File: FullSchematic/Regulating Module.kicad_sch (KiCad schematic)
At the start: 7 parts, among them U2 LM1117-3.3

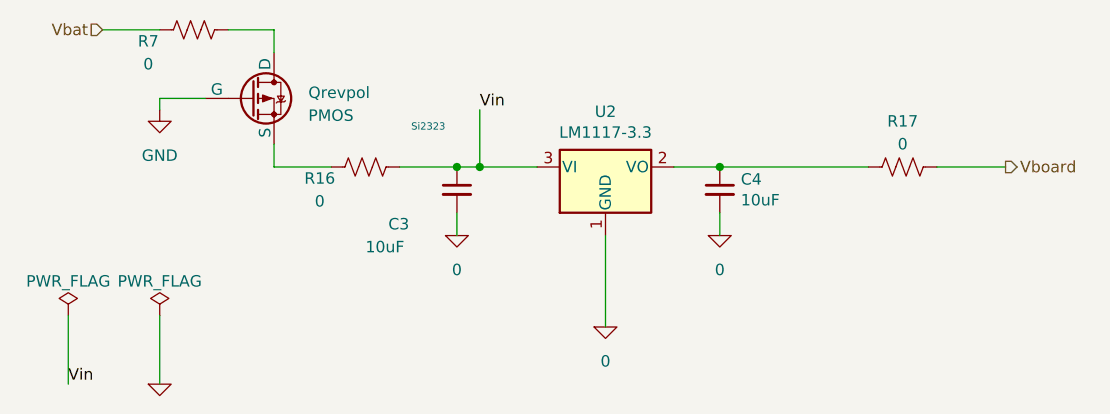
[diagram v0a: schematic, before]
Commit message: Added uvlo circuit
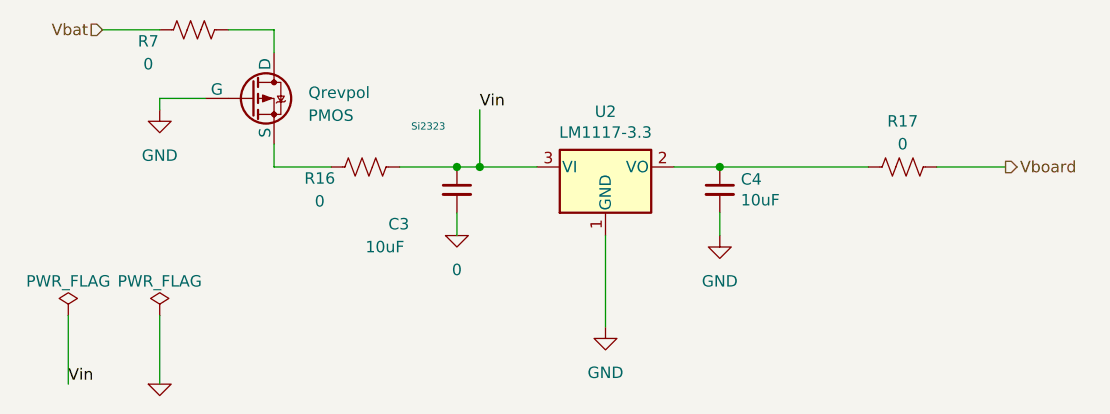
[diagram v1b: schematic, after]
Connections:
- net 0: no longer C4.2, U2.1 (GND)
- net GND: now also C4.2, U2.1 (GND)
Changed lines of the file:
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@@
-    )
-  )
-  (symbol (lib_id "Power module-rescue:0-pspice") (at 133.35 110.49 0) (unit 1)
-    (in_bom yes) (on_board yes) (dnp no)
-    (property "Reference" "#GND0106" (at 133.35 113.03 0)
-      (effects (font (size 1.27 1.27)) hide)
-    )
-    (property "Value" "0" (at 133.35 114.3 0)
-      (effects (font (size 1.27 1.27)))
-    )
-    (property "Footprint" "" (at 133.35 110.49 0)
-      (effects (font (size 1.27 1.27)) hide)
-    )
-    (property "Datasheet" "~" (at 133.35 110.49 0)
-      (effects (font (size 1.27 1.27)) hide)
-    )
-    (pin "1")
-    (instances
-      (project "Power module"
-        (path "/4323dbc9-3623-4dbc-9566-44afc0929253/00000000-0000-0000-0000-00006405027d"
-          (reference "#GND0106") (unit 1)
-        )
-      )
-      (project "FullSchematic"
-        (path "/5dd86611-a33d-45ee-946c-01c599f30b12/58d1f368-4b84-4dfe-a353-084728cf6b07/00000000-0000-0000-0000-00006405027d"
-          (reference "#GND0106") (unit 1)
-        )
-      )
     )
   )
@@
     )
   )
-  (symbol (lib_id "Power module-rescue:0-pspice") (at 146.05 100.33 0) (unit 1)
-    (in_bom yes) (on_board yes) (dnp no)
-    (property "Reference" "#GND0108" (at 146.05 102.87 0)
-      (effects (font (size 1.27 1.27)) hide)
-    )
-    (property "Value" "0" (at 146.05 104.14 0)
-      (effects (font (size 1.27 1.27)))
-    )
-    (property "Footprint" "" (at 146.05 100.33 0)
-      (effects (font (size 1.27 1.27)) hide)
-    )
-    (property "Datasheet" "~" (at 146.05 100.33 0)
-      (effects (font (size 1.27 1.27)) hide)
-    )
-    (pin "1")
-    (instances
-      (project "Power module"
-        (path "/4323dbc9-3623-4dbc-9566-44afc0929253/00000000-0000-0000-0000-00006405027d"
-          (reference "#GND0108") (unit 1)
-        )
-      )
-      (project "FullSchematic"
-        (path "/5dd86611-a33d-45ee-946c-01c599f30b12/58d1f368-4b84-4dfe-a353-084728cf6b07/00000000-0000-0000-0000-00006405027d"
-          (reference "#GND0108") (unit 1)
-        )
-      )
-    )
-  )
   (symbol (lib_id "Device:R_US") (at 166.37 92.71 90) (unit 1)
     (in_bom yes) (on_board yes) (dnp no) (fields_autoplaced)
@@
         )
       )
+    )
+  )
+  (symbol (lib_id "power:GND") (at 133.35 110.49 0) (unit 1)
+    (in_bom yes) (on_board yes) (dnp no) (fields_autoplaced)
+    (property "Reference" "#PWR04" (at 133.35 116.84 0)
+      (effects (font (size 1.27 1.27)) hide)
+    )
+    (property "Value" "GND" (at 133.35 115.57 0)
+      (effects (font (size 1.27 1.27)))
+    )
+    (property "Footprint" "" (at 133.35 110.49 0)
+      (effects (font (size 1.27 1.27)) hide)
+    )
+    (property "Datasheet" "" (at 133.35 110.49 0)
+      (effects (font (size 1.27 1.27)) hide)
+    )
+    (pin "1")
+    (instances
+      (project "Power module"
+        (path "/4323dbc9-3623-4dbc-9566-44afc0929253/00000000-0000-0000-0000-0000640501de"
+          (reference "#PWR04") (unit 1)
+        )
+        (path "/4323dbc9-3623-4dbc-9566-44afc0929253/00000000-0000-0000-0000-00006405027d"
+          (reference "#PWR05") (unit 1)
+        )
+      )
+      (project "FullSchematic"
+        (path "/5dd86611-a33d-45ee-946c-01c599f30b12/58d1f368-4b84-4dfe-a353-084728cf6b07/00000000-0000-0000-0000-00006405027d"
+          (reference "#PWR016") (unit 1)
+        )
+      )
+    )
+  )
+  (symbol (lib_id "power:GND") (at 146.05 100.33 0) (unit 1)
+    (in_bom yes) (on_board yes) (dnp no) (fields_autoplaced)
+    (property "Reference" "#PWR04" (at 146.05 106.68 0)
+      (effects (font (size 1.27 1.27)) hide)
+    )
+    (property "Value" "GND" (at 146.05 105.41 0)
+      (effects (font (size 1.27 1.27)))
+    )
+    (property "Footprint" "" (at 146.05 100.33 0)
+      (effects (font (size 1.27 1.27)) hide)
+    )
+    (property "Datasheet" "" (at 146.05 100.33 0)
+      (effects (font (size 1.27 1.27)) hide)
+    )
+    (pin "1")
+    (instances
+      (project "Power module"
+        (path "/4323dbc9-3623-4dbc-9566-44afc0929253/00000000-0000-0000-0000-0000640501de"
+          (reference "#PWR04") (unit 1)
+        )
+        (path "/4323dbc9-3623-4dbc-9566-44afc0929253/00000000-0000-0000-0000-00006405027d"
+          (reference "#PWR05") (unit 1)
+        )
+      )
+      (project "FullSchematic"
+        (path "/5dd86611-a33d-45ee-946c-01c599f30b12/58d1f368-4b84-4dfe-a353-084728cf6b07/00000000-0000-0000-0000-00006405027d"
+          (reference "#PWR017") (unit 1)
+        )
+      )

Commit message: Confirmed part numbers and prices
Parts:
- C3, C4: footprint Library:CAPC1608X90N -> Capacitor_SMD:C_0603_1608Metric; Populate (none) -> Yes
- Qrevpol, U2: Populate (none) -> Yes
- R16, R17, R7: footprint Library:RESC2013X65N -> Resistor_SMD:R_1206_3216Metric; Populate (none) -> Yes
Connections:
- net 0: no longer C3.2
- net GND: now also C3.2
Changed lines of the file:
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@@
+      (effects (font (size 1.27 1.27)) hide)
+    )
+    (property "Populate" "Yes" (at 133.35 92.71 0)
       (effects (font (size 1.27 1.27)) hide)
     )
@@
       (effects (font (size 1.27 1.27)) (justify left))
     )
-    (property "Footprint" "Library:CAPC1608X90N" (at 116.84 95.25 0)
+    (property "Footprint" "Capacitor_SMD:C_0603_1608Metric" (at 116.84 95.25 0)
       (effects (font (size 1.27 1.27)) hide)
     )
@@
     )
     (property "JLCPCB Part #" "C1691" (at 116.84 95.25 0)
+      (effects (font (size 1.27 1.27)) hide)
+    )
+    (property "Populate" "Yes" (at 116.84 95.25 0)
       (effects (font (size 1.27 1.27)) hide)
     )
@@
       (effects (font (size 1.27 1.27)) (justify left))
     )
-    (property "Footprint" "Library:CAPC1608X90N" (at 146.05 95.25 0)
+    (property "Footprint" "Capacitor_SMD:C_0603_1608Metric" (at 146.05 95.25 0)
       (effects (font (size 1.27 1.27)) hide)
     )
@@
       (effects (font (size 1.27 1.27)) hide)
     )
+    (property "Populate" "Yes" (at 146.05 95.25 0)
+      (effects (font (size 1.27 1.27)) hide)
+    )
     (pin "1")
     (pin "2")
@@
     )
   )
-  (symbol (lib_id "Power module-rescue:0-pspice") (at 116.84 100.33 0) (unit 1)
-    (in_bom yes) (on_board yes) (dnp no)
-    (property "Reference" "#GND0107" (at 116.84 102.87 0)
-      (effects (font (size 1.27 1.27)) hide)
-    )
-    (property "Value" "0" (at 116.84 104.14 0)
-      (effects (font (size 1.27 1.27)))
-    )
-    (property "Footprint" "" (at 116.84 100.33 0)
-      (effects (font (size 1.27 1.27)) hide)
-    )
-    (property "Datasheet" "~" (at 116.84 100.33 0)
-      (effects (font (size 1.27 1.27)) hide)
-    )
-    (pin "1")
-    (instances
-      (project "Power module"
-        (path "/4323dbc9-3623-4dbc-9566-44afc0929253/00000000-0000-0000-0000-00006405027d"
-          (reference "#GND0107") (unit 1)
-        )
-      )
-      (project "FullSchematic"
-        (path "/5dd86611-a33d-45ee-946c-01c599f30b12/58d1f368-4b84-4dfe-a353-084728cf6b07/00000000-0000-0000-0000-00006405027d"
-          (reference "#GND0107") (unit 1)
-        )
-      )
-    )
-  )
   (symbol (lib_id "Device:R_US") (at 166.37 92.71 90) (unit 1)
     (in_bom yes) (on_board yes) (dnp no) (fields_autoplaced)
@@
       (effects (font (size 1.27 1.27)))
     )
-    (property "Footprint" "Library:RESC2013X65N" (at 166.624 91.694 90)
+    (property "Footprint" "Resistor_SMD:R_1206_3216Metric" (at 166.624 91.694 90)
       (effects (font (size 1.27 1.27)) hide)
     )
@@
       (effects (font (size 1.27 1.27)) hide)
     )
+    (property "Populate" "Yes" (at 166.37 92.71 0)
+      (effects (font (size 1.27 1.27)) hide)
+    )
     (pin "1")
     (pin "2")
@@
     )
     (property "Price" "0.09" (at 93.98 85.09 0)
+      (effects (font (size 1.27 1.27)) hide)
+    )
+    (property "Populate" "Yes" (at 93.98 85.09 0)
       (effects (font (size 1.27 1.27)) hide)
     )
@@
       (effects (font (size 1.27 1.27)))
     )
-    (property "Footprint" "Library:RESC2013X65N" (at 87.884 76.454 90)
+    (property "Footprint" "Resistor_SMD:R_1206_3216Metric" (at 87.884 76.454 90)
       (effects (font (size 1.27 1.27)) hide)
     )
@@
     )
     (property "Price (5 boards)" "0.06" (at 87.63 77.47 0)
+      (effects (font (size 1.27 1.27)) hide)
+    )
+    (property "Populate" "Yes" (at 87.63 77.47 0)
       (effects (font (size 1.27 1.27)) hide)
     )
@@
       (effects (font (size 1.27 1.27)))
     )
-    (property "Footprint" "Library:RESC2013X65N" (at 106.934 91.694 90)
+    (property "Footprint" "Resistor_SMD:R_1206_3216Metric" (at 106.934 91.694 90)
       (effects (font (size 1.27 1.27)) hide)
     )
@@
       (effects (font (size 1.27 1.27)) hide)
     )
+    (property "Populate" "Yes" (at 106.68 92.71 0)
+      (effects (font (size 1.27 1.27)) hide)
+    )
     (pin "1")
     (pin "2")
@@
         )
       )
+    )
+  )
+  (symbol (lib_id "power:GND") (at 116.84 100.33 0) (unit 1)
+    (in_bom yes) (on_board yes) (dnp no) (fields_autoplaced)
+    (property "Reference" "#PWR021" (at 116.84 106.68 0)
+      (effects (font (size 1.27 1.27)) hide)
+    )
+    (property "Value" "GND" (at 116.84 105.41 0)
+      (effects (font (size 1.27 1.27)))
+    )
+    (property "Footprint" "" (at 116.84 100.33 0)
+      (effects (font (size 1.27 1.27)) hide)
+    )
+    (property "Datasheet" "" (at 116.84 100.33 0)
+      (effects (font (size 1.27 1.27)) hide)
+    )
+    (pin "1")
+    (instances
+      (project "FullSchematic"
+        (path "/5dd86611-a33d-45ee-946c-01c599f30b12/58d1f368-4b84-4dfe-a353-084728cf6b07/00000000-0000-0000-0000-00006405027d"
+          (reference "#PWR021") (unit 1)
+        )
+      )

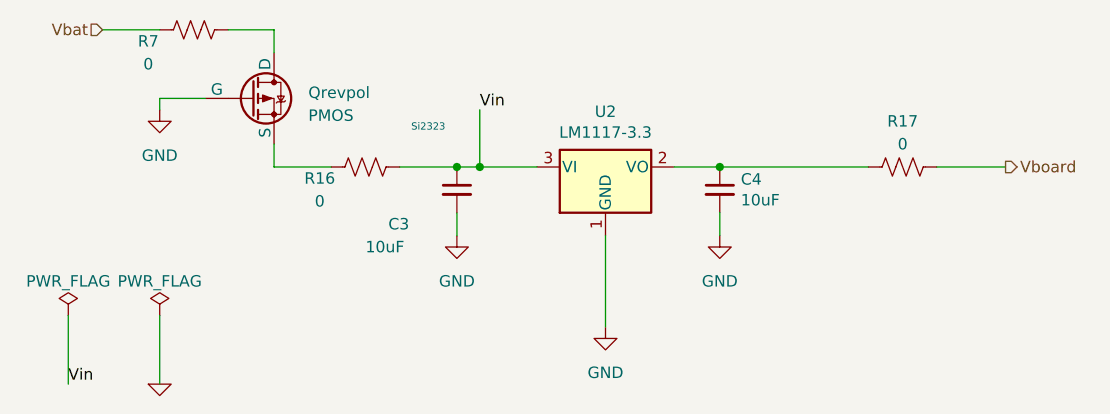
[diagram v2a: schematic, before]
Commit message: Checked part #s, prices, footprints
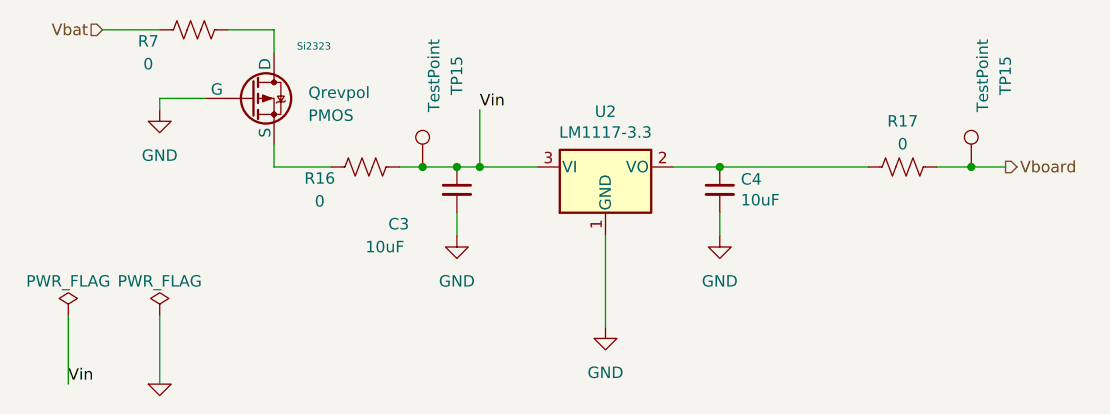
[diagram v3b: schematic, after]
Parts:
- added TP15 (x2): TestPoint, TestPoint:TestPoint_Pad_D2.0mm, symbol Connector:TestPoint
- C3: Price 0.08 -> 0.0052; Price ( 1 board) 0.24 -> 0.0208; Price (5 boards) 1.20 -> 0.104
- C4: Price 0.01 -> 0.0052; Price ( 1 board) 0.01 -> 0.0208; Price (5 boards) 0.05 -> 0.104
- Qrevpol: Price 0.09 -> 0.0721; Price ( 1 board) 0.18 -> 0.1442; Price (5 boards) 0.9 -> 0.721
- R16, R17, R7: Price ( 1 board) 0.012 -> 0.018; Price (5 boards) 0.06 -> 0.09
- U2: Price 0.072 -> 0.1455; Price ( 1 board) 0.072 -> 0.1455; Price (5 boards) 0.36 -> 0.7275
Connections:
- net Vboard: now also TP15.1
- net Vin: now also TP15.1
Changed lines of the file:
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@@
   (junction (at 146.05 92.71) (diameter 0) (color 0 0 0 0)
   )
+  (junction (at 113.03 92.71) (diameter 0) (color 0 0 0 0)
+  )
+  (junction (at 173.99 92.71) (diameter 0) (color 0 0 0 0)
+  )
   (junction (at 116.84 92.71) (diameter 0) (color 0 0 0 0)
   )
@@
     (stroke (width 0) (type default))
   )
-  (wire (pts (xy 110.49 92.71) (xy 116.84 92.71))
+  (wire (pts (xy 110.49 92.71) (xy 113.03 92.71))
     (stroke (width 0) (type default))
   )
@@
     (stroke (width 0) (type default))
   )
+  (wire (pts (xy 173.99 92.71) (xy 177.8 92.71))
+    (stroke (width 0) (type default))
+  )
   (wire (pts (xy 77.47 77.47) (xy 83.82 77.47))
     (stroke (width 0) (type default))
@@
     (stroke (width 0) (type default))
   )
-  (wire (pts (xy 170.18 92.71) (xy 177.8 92.71))
+  (wire (pts (xy 170.18 92.71) (xy 173.99 92.71))
     (stroke (width 0) (type default))
   )
@@
     (stroke (width 0) (type default))
   )
+  (wire (pts (xy 113.03 92.71) (xy 116.84 92.71))
+    (stroke (width 0) (type default))
+  )
   (wire (pts (xy 73.66 109.22) (xy 73.66 116.84))
     (stroke (width 0) (type default))
@@
     (stroke (width 0) (type default))
   )
-  (text "Si2323" (at 111.76 88.9 0)
+  (text "Si2323" (at 99.06 80.01 0)
     (effects (font (size 0.8 0.8)) (justify left bottom))
   )
@@
       (effects (font (size 1.27 1.27)) hide)
     )
-    (property "Price" "0.072" (at 133.35 92.71 0)
-      (effects (font (size 1.27 1.27)) hide)
-    )
-    (property "Price ( 1 board)" "0.072" (at 133.35 92.71 0)
-      (effects (font (size 1.27 1.27)) hide)
-    )
-    (property "Price (5 boards)" "0.36" (at 133.35 92.71 0)
+    (property "Price" "0.1455" (at 133.35 92.71 0)
+      (effects (font (size 1.27 1.27)) hide)
+    )
+    (property "Price ( 1 board)" "0.1455" (at 133.35 92.71 0)
+      (effects (font (size 1.27 1.27)) hide)
+    )
+    (property "Price (5 boards)" "0.7275" (at 133.35 92.71 0)
       (effects (font (size 1.27 1.27)) hide)
     )
@@
       (effects (font (size 1.27 1.27)) hide)
     )
-    (property "Price" "0.08" (at 116.84 95.25 0)
-      (effects (font (size 1.27 1.27)) hide)
-    )
-    (property "Price ( 1 board)" "0.24" (at 116.84 95.25 0)
-      (effects (font (size 1.27 1.27)) hide)
-    )
-    (property "Price (5 boards)" "1.20" (at 116.84 95.25 0)
+    (property "Price" "0.0052" (at 116.84 95.25 0)
+      (effects (font (size 1.27 1.27)) hide)
+    )
+    (property "Price ( 1 board)" "0.0208" (at 116.84 95.25 0)
+      (effects (font (size 1.27 1.27)) hide)
+    )
+    (property "Price (5 boards)" "0.104" (at 116.84 95.25 0)
       (effects (font (size 1.27 1.27)) hide)
     )
@@
       (effects (font (size 1.27 1.27)) hide)
     )
-    (property "Price" "0.01" (at 146.05 95.25 0)
-      (effects (font (size 1.27 1.27)) hide)
-    )
-    (property "Price ( 1 board)" "0.01" (at 146.05 95.25 0)
-      (effects (font (size 1.27 1.27)) hide)
-    )
-    (property "Price (5 boards)" "0.05" (at 146.05 95.25 0)
+    (property "Price" "0.0052" (at 146.05 95.25 0)
+      (effects (font (size 1.27 1.27)) hide)
+    )
+    (property "Price ( 1 board)" "0.0208" (at 146.05 95.25 0)
+      (effects (font (size 1.27 1.27)) hide)
+    )
+    (property "Price (5 boards)" "0.104" (at 146.05 95.25 0)
       (effects (font (size 1.27 1.27)) hide)
     )
@@
       (effects (font (size 1.27 1.27)) hide)
     )
-    (property "Price ( 1 board)" "0.012" (at 166.37 92.71 0)
-      (effects (font (size 1.27 1.27)) hide)
-    )
-    (property "Price (5 boards)" "0.06" (at 166.37 92.71 0)
+    (property "Price ( 1 board)" "0.018" (at 166.37 92.71 0)
+      (effects (font (size 1.27 1.27)) hide)
+    )
+    (property "Price (5 boards)" "0.09" (at 166.37 92.71 0)
       (effects (font (size 1.27 1.27)) hide)
     )
@@
       (effects (font (size 1.27 1.27)) hide)
     )
-    (property "Price ( 1 board)" "0.18" (at 93.98 85.09 0)
-      (effects (font (size 1.27 1.27)) hide)
-    )
-    (property "Price (5 boards)" "0.9" (at 93.98 85.09 0)
+    (property "Price ( 1 board)" "0.1442" (at 93.98 85.09 0)
+      (effects (font (size 1.27 1.27)) hide)
+    )
+    (property "Price (5 boards)" "0.721" (at 93.98 85.09 0)
       (effects (font (size 1.27 1.27)) hide)
     )
@@
       (effects (font (size 1.27 1.27)) hide)
     )
-    (property "Price" "0.09" (at 93.98 85.09 0)
+    (property "Price" "0.0721" (at 93.98 85.09 0)
       (effects (font (size 1.27 1.27)) hide)
     )
@@
       (effects (font (size 1.27 1.27)) hide)
     )
-    (property "Price ( 1 board)" "0.012" (at 87.63 77.47 0)
-      (effects (font (size 1.27 1.27)) hide)
-    )
-    (property "Price (5 boards)" "0.06" (at 87.63 77.47 0)
+    (property "Price ( 1 board)" "0.018" (at 87.63 77.47 0)
+      (effects (font (size 1.27 1.27)) hide)
+    )
+    (property "Price (5 boards)" "0.09" (at 87.63 77.47 0)
       (effects (font (size 1.27 1.27)) hide)
     )
@@
     )
   )
+  (symbol (lib_id "Connector:TestPoint") (at 113.03 92.71 0) (unit 1)
+    (in_bom yes) (on_board yes) (dnp no)
+    (property "Reference" "TP15" (at 116.84 82.55 90)
+      (effects (font (size 1.27 1.27)))
+    )
+    (property "Value" "TestPoint" (at 114.3 82.55 90)
+      (effects (font (size 1.27 1.27)))
+    )
+    (property "Footprint" "TestPoint:TestPoint_Pad_D2.0mm" (at 118.11 92.71 0)
+      (effects (font (size 1.27 1.27)) hide)
+    )
+    (property "Datasheet" "~" (at 118.11 92.71 0)
+      (effects (font (size 1.27 1.27)) hide)
+    )
+    (property "Price" "$0" (at 113.03 92.71 0)
+      (effects (font (size 1.27 1.27)) hide)
+    )
+    (property "Price ( 1 board)" "0" (at 113.03 92.71 0)
+      (effects (font (size 1.27 1.27)) hide)
+    )
+    (property "Price (5 boards)" "0" (at 113.03 92.71 0)
+      (effects (font (size 1.27 1.27)) hide)
+    )
+    (property "JLCPCB Part #" "N/A" (at 113.03 92.71 0)
+      (effects (font (size 1.27 1.27)) hide)
+    )
+    (pin "1")
+    (instances
+      (project "FullSchematic"
+        (path "/5dd86611-a33d-45ee-946c-01c599f30b12/58d1f368-4b84-4dfe-a353-084728cf6b07/00000000-0000-0000-0000-0000640501de"
+          (reference "TP15") (unit 1)
+        )
+        (path "/5dd86611-a33d-45ee-946c-01c599f30b12/58d1f368-4b84-4dfe-a353-084728cf6b07/00000000-0000-0000-0000-00006405027d"
+          (reference "TP22") (unit 1)
+        )
+      )
+    )
+  )
   (symbol (lib_id "power:GND") (at 146.05 100.33 0) (unit 1)
     (in_bom yes) (on_board yes) (dnp no) (fields_autoplaced)
@@
       (effects (font (size 1.27 1.27)) hide)
     )
-    (property "Price ( 1 board)" "0.012" (at 106.68 92.71 0)
-      (effects (font (size 1.27 1.27)) hide)
-    )
-    (property "Price (5 boards)" "0.06" (at 106.68 92.71 0)
+    (property "Price ( 1 board)" "0.018" (at 106.68 92.71 0)
+      (effects (font (size 1.27 1.27)) hide)
+    )
+    (property "Price (5 boards)" "0.09" (at 106.68 92.71 0)
       (effects (font (size 1.27 1.27)) hide)
     )
@@
         )
       )
+    )
+  )
+  (symbol (lib_id "Connector:TestPoint") (at 173.99 92.71 0) (unit 1)
+    (in_bom yes) (on_board yes) (dnp no)
+    (property "Reference" "TP15" (at 177.8 82.55 90)
+      (effects (font (size 1.27 1.27)))
+    )
+    (property "Value" "TestPoint" (at 175.26 82.55 90)
+      (effects (font (size 1.27 1.27)))
+    )
+    (property "Footprint" "TestPoint:TestPoint_Pad_D2.0mm" (at 179.07 92.71 0)
+      (effects (font (size 1.27 1.27)) hide)
+    )
+    (property "Datasheet" "~" (at 179.07 92.71 0)
+      (effects (font (size 1.27 1.27)) hide)
+    )
+    (property "Price" "$0" (at 173.99 92.71 0)
+      (effects (font (size 1.27 1.27)) hide)
+    )
+    (property "Price ( 1 board)" "0" (at 173.99 92.71 0)
+      (effects (font (size 1.27 1.27)) hide)
+    )
+    (property "Price (5 boards)" "0" (at 173.99 92.71 0)
+      (effects (font (size 1.27 1.27)) hide)
+    )
+    (property "JLCPCB Part #" "N/A" (at 173.99 92.71 0)
+      (effects (font (size 1.27 1.27)) hide)
+    )
+    (pin "1")
+    (instances
+      (project "FullSchematic"
+        (path "/5dd86611-a33d-45ee-946c-01c599f30b12/58d1f368-4b84-4dfe-a353-084728cf6b07/00000000-0000-0000-0000-0000640501de"
+          (reference "TP15") (unit 1)
+        )
+        (path "/5dd86611-a33d-45ee-946c-01c599f30b12/58d1f368-4b84-4dfe-a353-084728cf6b07/00000000-0000-0000-0000-00006405027d"
+          (reference "TP23") (unit 1)
+        )
+      )

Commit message: Final Board
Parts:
- U2: footprint Library:SOT230P700X180-4N -> Package_TO_SOT_SMD:SOT-223
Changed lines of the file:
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@@
       (effects (font (size 1.27 1.27)))
     )
-    (property "Footprint" "Library:SOT230P700X180-4N" (at 133.35 92.71 0)
+    (property "Footprint" "Package_TO_SOT_SMD:SOT-223" (at 133.35 92.71 0)
       (effects (font (size 1.27 1.27)) hide)
     )
